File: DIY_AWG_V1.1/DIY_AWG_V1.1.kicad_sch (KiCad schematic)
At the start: 0 parts

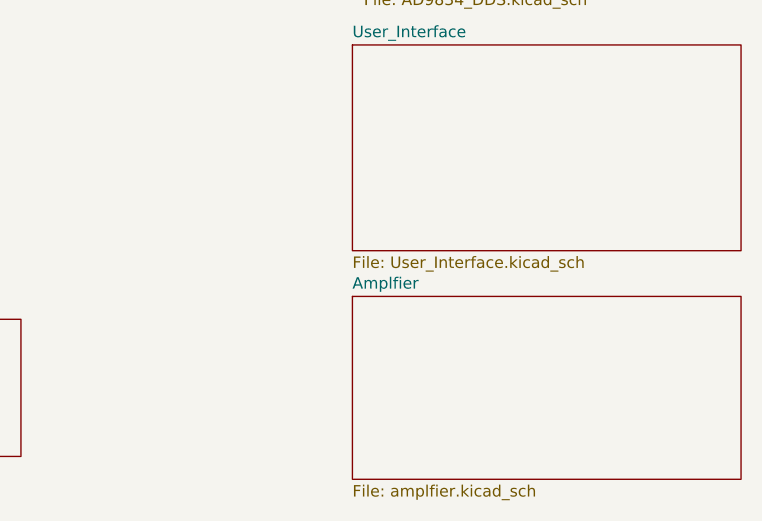
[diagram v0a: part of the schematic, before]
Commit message: Updated power_supply schematics
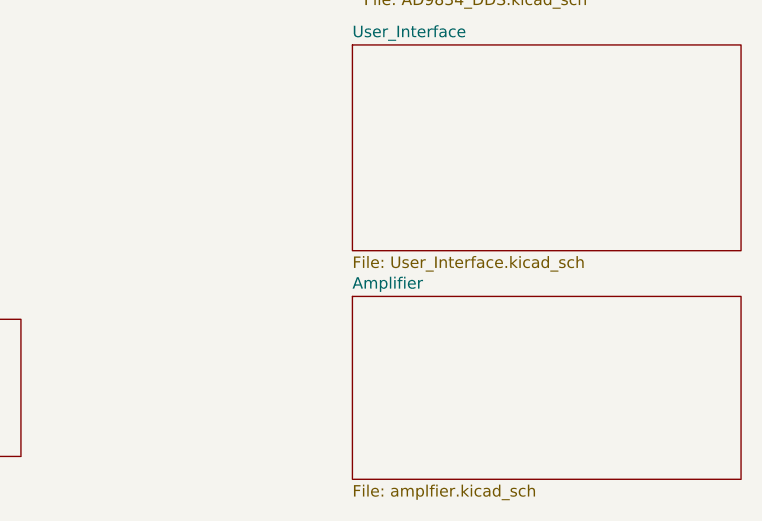
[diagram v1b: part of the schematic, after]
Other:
- sheet Amplfier renamed Amplifier
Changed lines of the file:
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@@
 			(color 0 0 0 0)
 		)
-		(property "Sheetname" "Amplfier"
+		(property "Sheetname" "Amplifier"
 			(at 238.76 126.2884 0)
 			(show_name no)

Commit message: Updated STM32_MCU, amplifier, User_Interface, AD9834_DDS schematic
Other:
- removed sheet Temp
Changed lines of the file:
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@@
-	)
-	(sheet
-		(at 166.37 129.54)
-		(size 35.56 15.24)
-		(exclude_from_sim no)
-		(in_bom yes)
-		(on_board yes)
-		(dnp no)
-		(fields_autoplaced yes)
-		(stroke
-			(width 0.1524)
-			(type solid)
-		)
-		(fill
-			(color 0 0 0 0)
-		)
-		(property "Sheetname" "Temp"
-			(at 166.37 128.8284 0)
-			(show_name no)
-			(do_not_autoplace no)
-			(effects
-				(font
-					(size 1.27 1.27)
-				)
-				(justify left bottom)
-			)
-		)
-		(property "Sheetfile" "temp.kicad_sch"
-			(at 166.37 145.3646 0)
-			(show_name no)
-			(do_not_autoplace no)
-			(effects
-				(font
-					(size 1.27 1.27)
-				)
-				(justify left top)
-			)
-		)
-		(instances
-			(project "DIY_AWG_V1.1"
-				(path "/508078af-d961-4af3-840e-a064a9f8d5bc"
-					(page "6")
-				)
-			)
-		)
 	)
 	(sheet

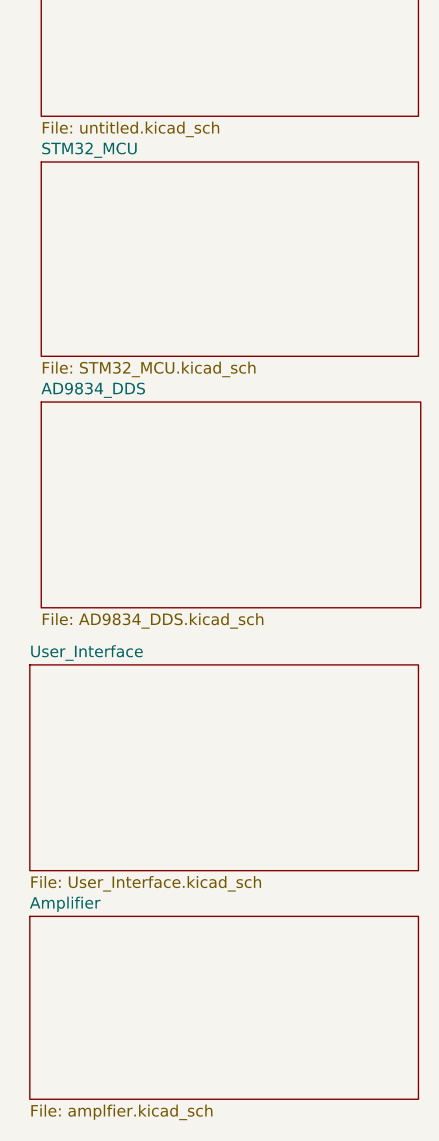
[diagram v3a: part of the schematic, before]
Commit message: Updated pin description of relevant components
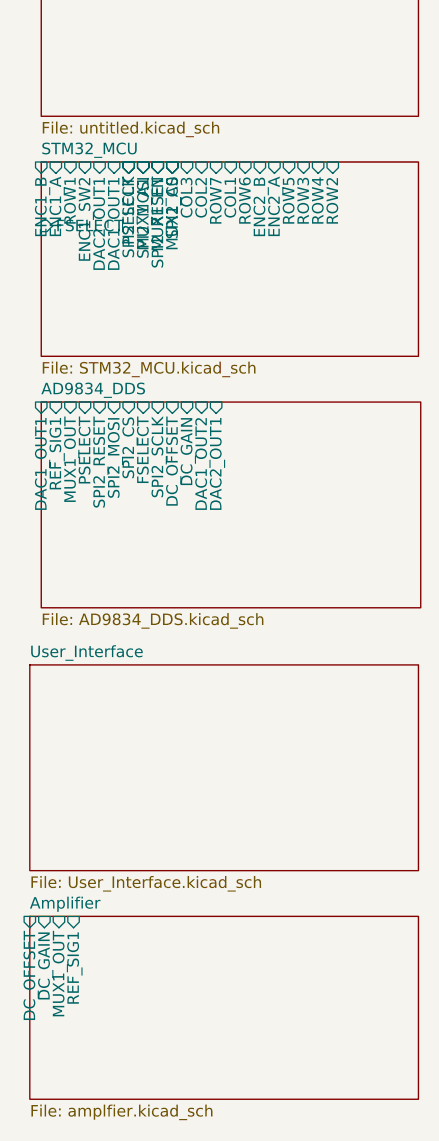
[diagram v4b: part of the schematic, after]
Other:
- sheet AD9834_DDS ports: added DAC1_OUT1, DAC1_OUT2, DAC2_OUT1, DC_GAIN, DC_OFFSET, FSELECT, MUX1_OUT, PSELECT, REF_SIG1, SPI2_CS, SPI2_MOSI, SPI2_RESET, SPI2_SCLK; removed none
- sheet Amplifier ports: added DC_GAIN, DC_OFFSET, MUX1_OUT, REF_SIG1; removed none
- sheet STM32_MCU ports: added COL1, COL2, COL3, DAC1_OUT1, DAC2_OUT1, ENC1_A, ENC1_B, ENC1_SW2, ENC2_A, ENC2_B, FSELECT, MUX1_A0, MUX1_A1, MUX1_EN, PSELECT, ROW1, ROW2, ROW3, ROW4, ROW5, ROW6, ROW7, SPI2_CS, SPI2_MOSI, SPI2_RESET, SPI2_SCLK; removed none

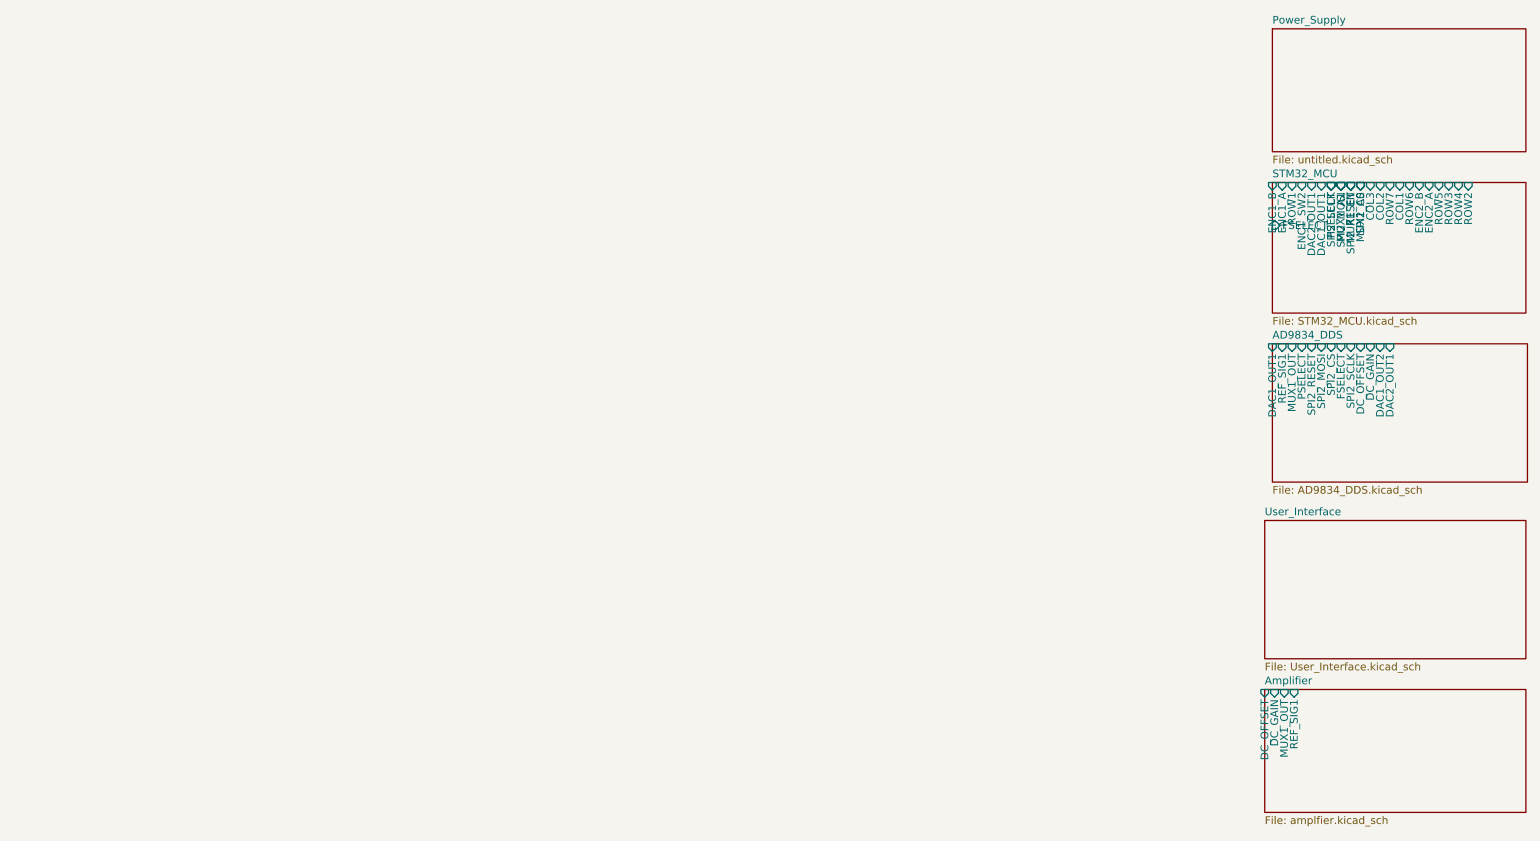
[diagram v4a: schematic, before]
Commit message: Updated schematics to clear ERCs
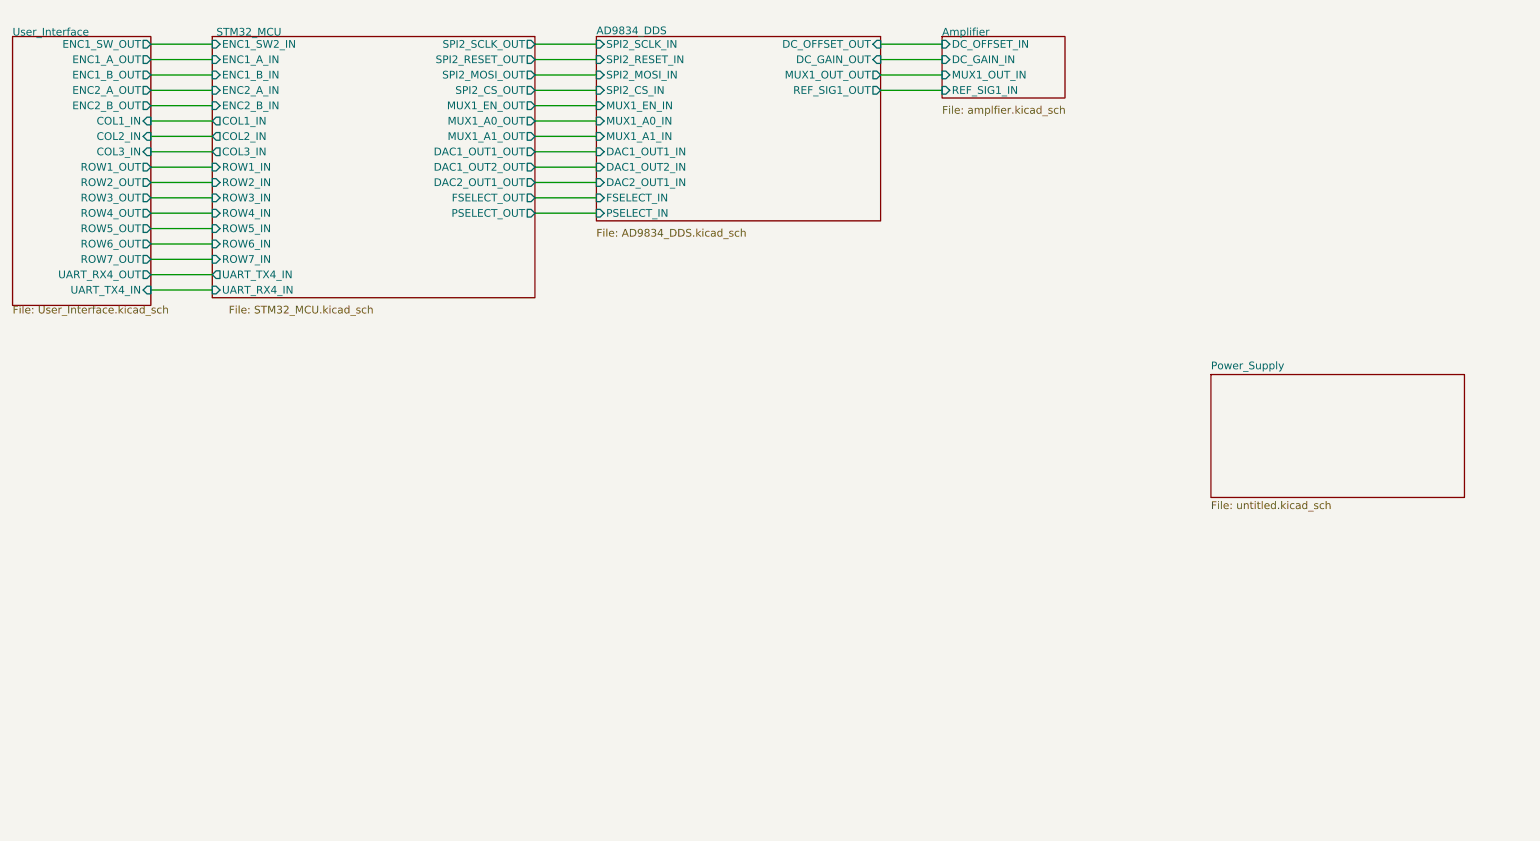
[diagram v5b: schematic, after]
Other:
- sheet AD9834_DDS ports: added DAC1_OUT1_IN, DAC1_OUT2_IN, DAC2_OUT1_IN, DC_GAIN_OUT, DC_OFFSET_OUT, FSELECT_IN, MUX1_A0_IN, MUX1_A1_IN, MUX1_EN_IN, MUX1_OUT_OUT, PSELECT_IN, REF_SIG1_OUT, SPI2_CS_IN, SPI2_MOSI_IN, SPI2_RESET_IN, SPI2_SCLK_IN; removed DAC1_OUT1, DAC1_OUT2, DAC2_OUT1, DC_GAIN, DC_OFFSET, FSELECT, MUX1_OUT, PSELECT, REF_SIG1, SPI2_CS, SPI2_MOSI, SPI2_RESET, SPI2_SCLK
- sheet Amplifier ports: added DC_GAIN_IN, DC_OFFSET_IN, MUX1_OUT_IN, REF_SIG1_IN; removed DC_GAIN, DC_OFFSET, MUX1_OUT, REF_SIG1
- sheet STM32_MCU ports: added COL1_IN, COL2_IN, COL3_IN, DAC1_OUT1_OUT, DAC1_OUT2_OUT, DAC2_OUT1_OUT, ENC1_A_IN, ENC1_B_IN, ENC1_SW2_IN, ENC2_A_IN, ENC2_B_IN, FSELECT_OUT, MUX1_A0_OUT, MUX1_A1_OUT, MUX1_EN_OUT, PSELECT_OUT, ROW1_IN, ROW2_IN, ROW3_IN, ROW4_IN, ROW5_IN, ROW6_IN, ROW7_IN, SPI2_CS_OUT, SPI2_MOSI_OUT, SPI2_RESET_OUT, SPI2_SCLK_OUT, UART_RX4_IN, UART_TX4_IN; removed COL1, COL2, COL3, DAC1_OUT1, DAC2_OUT1, ENC1_A, ENC1_B, ENC1_SW2, ENC2_A, ENC2_B, FSELECT, MUX1_A0, MUX1_A1, MUX1_EN, PSELECT, ROW1, ROW2, ROW3, ROW4, ROW5, ROW6, ROW7, SPI2_CS, SPI2_MOSI, SPI2_RESET, SPI2_SCLK
- sheet User_Interface ports: added COL1_IN, COL2_IN, COL3_IN, ENC1_A_OUT, ENC1_B_OUT, ENC1_SW_OUT, ENC2_A_OUT, ENC2_B_OUT, ROW1_OUT, ROW2_OUT, ROW3_OUT, ROW4_OUT, ROW5_OUT, ROW6_OUT, ROW7_OUT, UART_RX4_OUT, UART_TX4_IN; removed none

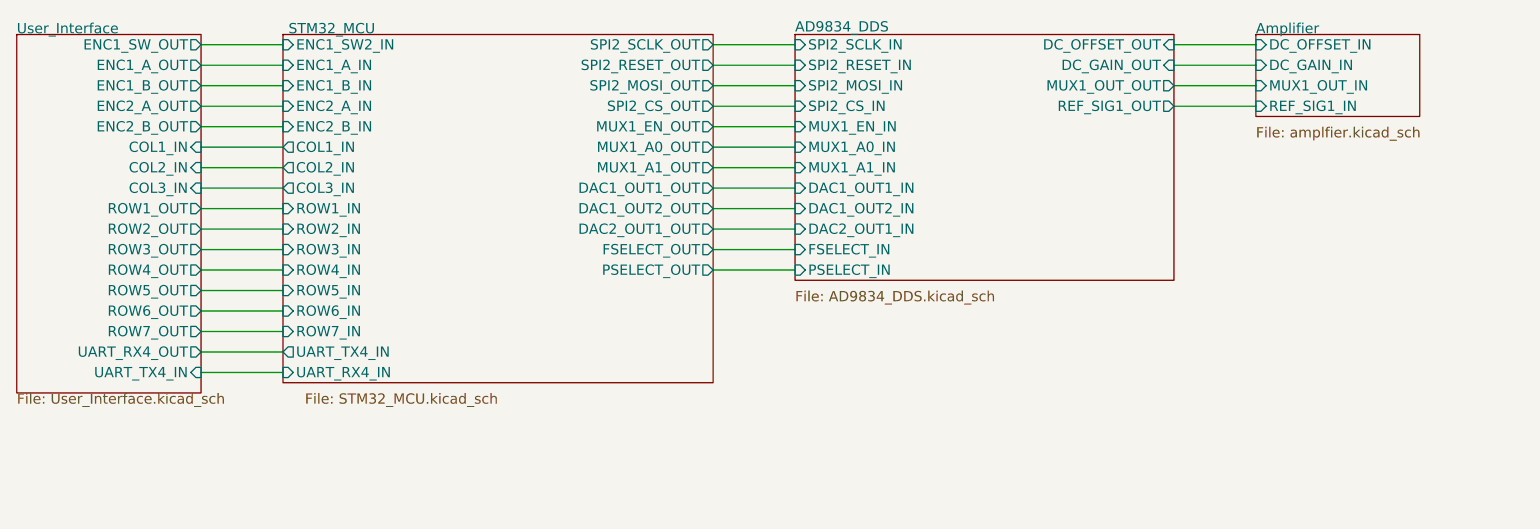
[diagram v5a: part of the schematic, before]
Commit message: Updated schematics to clear ERCs
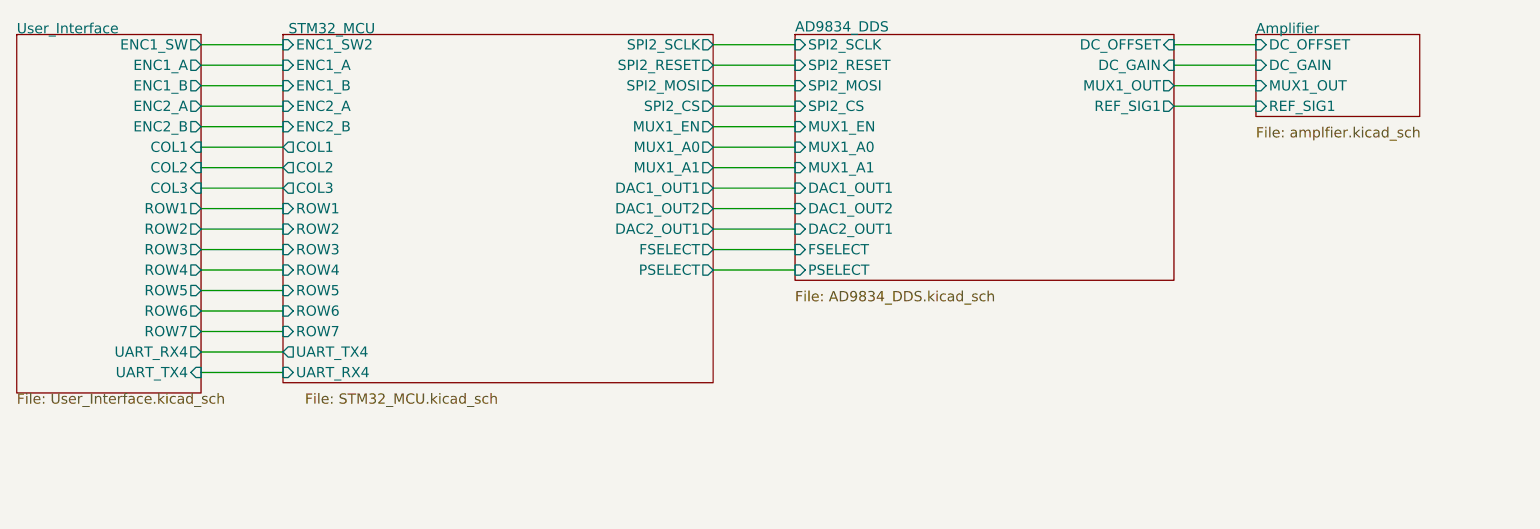
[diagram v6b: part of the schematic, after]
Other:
- sheet AD9834_DDS ports: added DAC1_OUT1, DAC1_OUT2, DAC2_OUT1, DC_GAIN, DC_OFFSET, FSELECT, MUX1_A0, MUX1_A1, MUX1_EN, MUX1_OUT, PSELECT, REF_SIG1, SPI2_CS, SPI2_MOSI, SPI2_RESET, SPI2_SCLK; removed DAC1_OUT1_IN, DAC1_OUT2_IN, DAC2_OUT1_IN, DC_GAIN_OUT, DC_OFFSET_OUT, FSELECT_IN, MUX1_A0_IN, MUX1_A1_IN, MUX1_EN_IN, MUX1_OUT_OUT, PSELECT_IN, REF_SIG1_OUT, SPI2_CS_IN, SPI2_MOSI_IN, SPI2_RESET_IN, SPI2_SCLK_IN
- sheet Amplifier ports: added DC_GAIN, DC_OFFSET, MUX1_OUT, REF_SIG1; removed DC_GAIN_IN, DC_OFFSET_IN, MUX1_OUT_IN, REF_SIG1_IN
- sheet STM32_MCU ports: added COL1, COL2, COL3, DAC1_OUT1, DAC1_OUT2, DAC2_OUT1, ENC1_A, ENC1_B, ENC1_SW2, ENC2_A, ENC2_B, FSELECT, MUX1_A0, MUX1_A1, MUX1_EN, PSELECT, ROW1, ROW2, ROW3, ROW4, ROW5, ROW6, ROW7, SPI2_CS, SPI2_MOSI, SPI2_RESET, SPI2_SCLK, UART_RX4, UART_TX4; removed COL1_IN, COL2_IN, COL3_IN, DAC1_OUT1_OUT, DAC1_OUT2_OUT, DAC2_OUT1_OUT, ENC1_A_IN, ENC1_B_IN, ENC1_SW2_IN, ENC2_A_IN, ENC2_B_IN, FSELECT_OUT, MUX1_A0_OUT, MUX1_A1_OUT, MUX1_EN_OUT, PSELECT_OUT, ROW1_IN, ROW2_IN, ROW3_IN, ROW4_IN, ROW5_IN, ROW6_IN, ROW7_IN, SPI2_CS_OUT, SPI2_MOSI_OUT, SPI2_RESET_OUT, SPI2_SCLK_OUT, UART_RX4_IN, UART_TX4_IN
- sheet User_Interface ports: added COL1, COL2, COL3, ENC1_A, ENC1_B, ENC1_SW, ENC2_A, ENC2_B, ROW1, ROW2, ROW3, ROW4, ROW5, ROW6, ROW7, UART_RX4, UART_TX4; removed COL1_IN, COL2_IN, COL3_IN, ENC1_A_OUT, ENC1_B_OUT, ENC1_SW_OUT, ENC2_A_OUT, ENC2_B_OUT, ROW1_OUT, ROW2_OUT, ROW3_OUT, ROW4_OUT, ROW5_OUT, ROW6_OUT, ROW7_OUT, UART_RX4_OUT, UART_TX4_IN
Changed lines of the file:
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@@
 			)
 		)
-		(pin "DAC1_OUT1_IN" input
+		(pin "DAC1_OUT1" input
 			(at 128.27 38.1 180)
 			(effects
@@
 			)
 		)
-		(pin "DAC1_OUT2_IN" input
+		(pin "DAC1_OUT2" input
 			(at 128.27 40.64 180)
 			(effects
@@
 			)
 		)
-		(pin "DAC2_OUT1_IN" input
+		(pin "DAC2_OUT1" input
 			(at 128.27 43.18 180)
 			(effects
@@
 			)
 		)
-		(pin "DC_GAIN_OUT" input
+		(pin "DC_GAIN" input
 			(at 175.26 22.86 0)
 			(effects
@@
 			)
 		)
-		(pin "DC_OFFSET_OUT" input
+		(pin "DC_OFFSET" input
 			(at 175.26 20.32 0)
 			(effects
@@
 			)
 		)
-		(pin "FSELECT_IN" input
+		(pin "FSELECT" input
 			(at 128.27 45.72 180)
 			(effects
@@
 			)
 		)
-		(pin "MUX1_A0_IN" input
+		(pin "MUX1_A0" input
 			(at 128.27 33.02 180)
 			(effects
@@
 			)
 		)
-		(pin "MUX1_A1_IN" input
+		(pin "MUX1_A1" input
 			(at 128.27 35.56 180)
 			(effects
@@
 			)
 		)
-		(pin "MUX1_EN_IN" input
+		(pin "MUX1_EN" input
 			(at 128.27 30.48 180)
 			(effects
@@
 			)
 		)
-		(pin "MUX1_OUT_OUT" output
+		(pin "MUX1_OUT" output
 			(at 175.26 25.4 0)
 			(effects
@@
 			)
 		)
-		(pin "PSELECT_IN" input
+		(pin "PSELECT" input
 			(at 128.27 48.26 180)
 			(effects
@@
 			)
 		)
-		(pin "REF_SIG1_OUT" output
+		(pin "REF_SIG1" output
 			(at 175.26 27.94 0)
 			(effects
@@
 			)
 		)
-		(pin "SPI2_CS_IN" input
+		(pin "SPI2_CS" input
 			(at 128.27 27.94 180)
 			(effects
@@
 			)
 		)
-		(pin "SPI2_MOSI_IN" input
+		(pin "SPI2_MOSI" input
 			(at 128.27 25.4 180)
 			(effects
@@
 			)
 		)
-		(pin "SPI2_RESET_IN" input
+		(pin "SPI2_RESET" input
 			(at 128.27 22.86 180)
 			(effects
@@
 			)
 		)
-		(pin "SPI2_SCLK_IN" input
+		(pin "SPI2_SCLK" input
 			(at 128.27 20.32 180)
 			(effects
@@
 			)
 		)
-		(pin "COL1_IN" input
+		(pin "COL1" input
 			(at 54.61 33.02 0)
 			(effects
@@
 			)
 		)
-		(pin "COL2_IN" input
+		(pin "COL2" input
 			(at 54.61 35.56 0)
 			(effects
@@
 			)
 		)
-		(pin "COL3_IN" input
+		(pin "COL3" input
 			(at 54.61 38.1 0)
 			(effects
@@
 			)
 		)
-		(pin "ENC1_A_OUT" output
+		(pin "ENC1_A" output
 			(at 54.61 22.86 0)
 			(effects
@@
 			)
 		)
-		(pin "ENC1_B_OUT" output
+		(pin "ENC1_B" output
 			(at 54.61 25.4 0)
 			(effects
@@
 			)
 		)
-		(pin "ENC1_SW_OUT" output
+		(pin "ENC1_SW" output
 			(at 54.61 20.32 0)
 			(effects
@@
 			)
 		)
-		(pin "ENC2_A_OUT" output
+		(pin "ENC2_A" output
 			(at 54.61 27.94 0)
 			(effects
@@
 			)
 		)
-		(pin "ENC2_B_OUT" output
+		(pin "ENC2_B" output
 			(at 54.61 30.48 0)
 			(effects
@@
 			)
 		)
-		(pin "ROW1_OUT" output
+		(pin "ROW1" output
 			(at 54.61 40.64 0)
 			(effects
@@
 			)
 		)
-		(pin "ROW2_OUT" output
+		(pin "ROW2" output
 			(at 54.61 43.18 0)
 			(effects
@@
 			)
 		)
-		(pin "ROW3_OUT" output
+		(pin "ROW3" output
 			(at 54.61 45.72 0)
 			(effects
@@
 			)
 		)
-		(pin "ROW4_OUT" output
+		(pin "ROW4" output
 			(at 54.61 48.26 0)
 			(effects
@@
 			)
 		)
-		(pin "ROW5_OUT" output
+		(pin "ROW5" output
 			(at 54.61 50.8 0)
 			(effects
@@
 			)
 		)
-		(pin "ROW6_OUT" output
+		(pin "ROW6" output
 			(at 54.61 53.34 0)
 			(effects
@@
 			)
 		)
-		(pin "ROW7_OUT" output
+		(pin "ROW7" output
 			(at 54.61 55.88 0)
 			(effects
@@
 			)
 		)
-		(pin "UART_RX4_OUT" output
+		(pin "UART_RX4" output
 			(at 54.61 58.42 0)
 			(effects
@@
 			)
 		)
-		(pin "UART_TX4_IN" input
+		(pin "UART_TX4" input
 			(at 54.61 60.96 0)
 			(effects
@@
 			)
 		)
-		(pin "COL1_IN" output
+		(pin "COL1" output
 			(at 64.77 33.02 180)
 			(effects
@@
 			)
 		)
-		(pin "COL2_IN" output
+		(pin "COL2" output
 			(at 64.77 35.56 180)
 			(effects
@@
 			)
 		)
-		(pin "COL3_IN" output
+		(pin "COL3" output
 			(at 64.77 38.1 180)
 			(effects
@@
 			)
 		)
-		(pin "DAC1_OUT1_OUT" output
+		(pin "DAC1_OUT1" output
 			(at 118.11 38.1 0)
 			(effects
@@
 			)
 		)
-		(pin "DAC1_OUT2_OUT" output
+		(pin "DAC1_OUT2" output
 			(at 118.11 40.64 0)
 			(effects
@@
 			)
 		)
-		(pin "DAC2_OUT1_OUT" output
+		(pin "DAC2_OUT1" output
 			(at 118.11 43.18 0)
 			(effects
@@
 			)
 		)
-		(pin "MUX1_A0_OUT" output
+		(pin "MUX1_A0" output
 			(at 118.11 33.02 0)
 			(effects
@@
 			)
 		)
-		(pin "MUX1_A1_OUT" output
+		(pin "MUX1_A1" output
 			(at 118.11 35.56 0)
 			(effects
@@
 			)
 		)
-		(pin "MUX1_EN_OUT" output
+		(pin "MUX1_EN" output
 			(at 118.11 30.48 0)
 			(effects
@@
 			)
 		)
-		(pin "ROW1_IN" input
+		(pin "ROW1" input
 			(at 64.77 40.64 180)
 			(effects
@@
 			)
 		)
-		(pin "ROW2_IN" input
+		(pin "ROW2" input
 			(at 64.77 43.18 180)
 			(effects
@@
 			)
 		)
-		(pin "ROW3_IN" input
+		(pin "ROW3" input
 			(at 64.77 45.72 180)
 			(effects
@@
 			)
 		)
-		(pin "ROW4_IN" input
+		(pin "ROW4" input
 			(at 64.77 48.26 180)
 			(effects
@@
 			)
 		)
-		(pin "ROW5_IN" input
+		(pin "ROW5" input
 			(at 64.77 50.8 180)
 			(effects
@@
 			)
 		)
-		(pin "ROW6_IN" input
+		(pin "ROW6" input
 			(at 64.77 53.34 180)
 			(effects
@@
 			)
 		)
-		(pin "ROW7_IN" input
+		(pin "ROW7" input
 			(at 64.77 55.88 180)
 			(effects
@@
 			)
 		)
-		(pin "SPI2_CS_OUT" output
+		(pin "SPI2_CS" output
 			(at 118.11 27.94 0)
 			(effects
@@
 			)
 		)
-		(pin "SPI2_MOSI_OUT" output
+		(pin "SPI2_MOSI" output
 			(at 118.11 25.4 0)
 			(effects
@@
 			)
 		)
-		(pin "SPI2_RESET_OUT" output
+		(pin "SPI2_RESET" output
 			(at 118.11 22.86 0)
 			(effects
@@
 			)
 		)
-		(pin "SPI2_SCLK_OUT" output
+		(pin "SPI2_SCLK" output
 			(at 118.11 20.32 0)
 			(effects
@@
 			)
 		)
-		(pin "UART_RX4_IN" input
+		(pin "UART_RX4" input
 			(at 64.77 60.96 180)
 			(effects
@@
 			)
 		)
-		(pin "UART_TX4_IN" output
+		(pin "UART_TX4" output
 			(at 64.77 58.42 180)
 			(effects
@@
 			)
 		)
-		(pin "ENC1_A_IN" input
+		(pin "ENC1_A" input
 			(at 64.77 22.86 180)
 			(effects
@@
 			)
 		)
-		(pin "ENC1_B_IN" input
+		(pin "ENC1_B" input
 			(at 64.77 25.4 180)
 			(effects
@@
 			)
 		)
-		(pin "ENC1_SW2_IN" input
+		(pin "ENC1_SW2" input
 			(at 64.77 20.32 180)
 			(effects
@@
 			)
 		)
-		(pin "ENC2_A_IN" input
+		(pin "ENC2_A" input
 			(at 64.77 27.94 180)
 			(effects
@@
 			)
 		)
-		(pin "ENC2_B_IN" input
+		(pin "ENC2_B" input
 			(at 64.77 30.48 180)
 			(effects
@@
 			)
 		)
-		(pin "FSELECT_OUT" output
+		(pin "FSELECT" output
 			(at 118.11 45.72 0)
 			(effects
@@
 			)
 		)
-		(pin "PSELECT_OUT" output
+		(pin "PSELECT" output
 			(at 118.11 48.26 0)
 			(effects
@@
 			)
 		)
-		(pin "DC_GAIN_IN" input
+		(pin "DC_GAIN" input
 			(at 185.42 22.86 180)
 			(effects
@@
 			)
 		)
-		(pin "DC_OFFSET_IN" input
+		(pin "DC_OFFSET" input
 			(at 185.42 20.32 180)
 			(effects
@@
 			)
 		)
-		(pin "MUX1_OUT_IN" input
+		(pin "MUX1_OUT" input
 			(at 185.42 25.4 180)
 			(effects
@@
 			)
 		)
-		(pin "REF_SIG1_IN" input
+		(pin "REF_SIG1" input
 			(at 185.42 27.94 180)
 			(effects
